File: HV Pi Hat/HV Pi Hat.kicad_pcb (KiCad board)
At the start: 4 copper layers, 85 x 56 mm, 20 parts, among them J1 B2B-XH-A_LF__SN_, J2 B2B-XH-A_LF__SN_, J3 SHV-R, J4 SHV-R

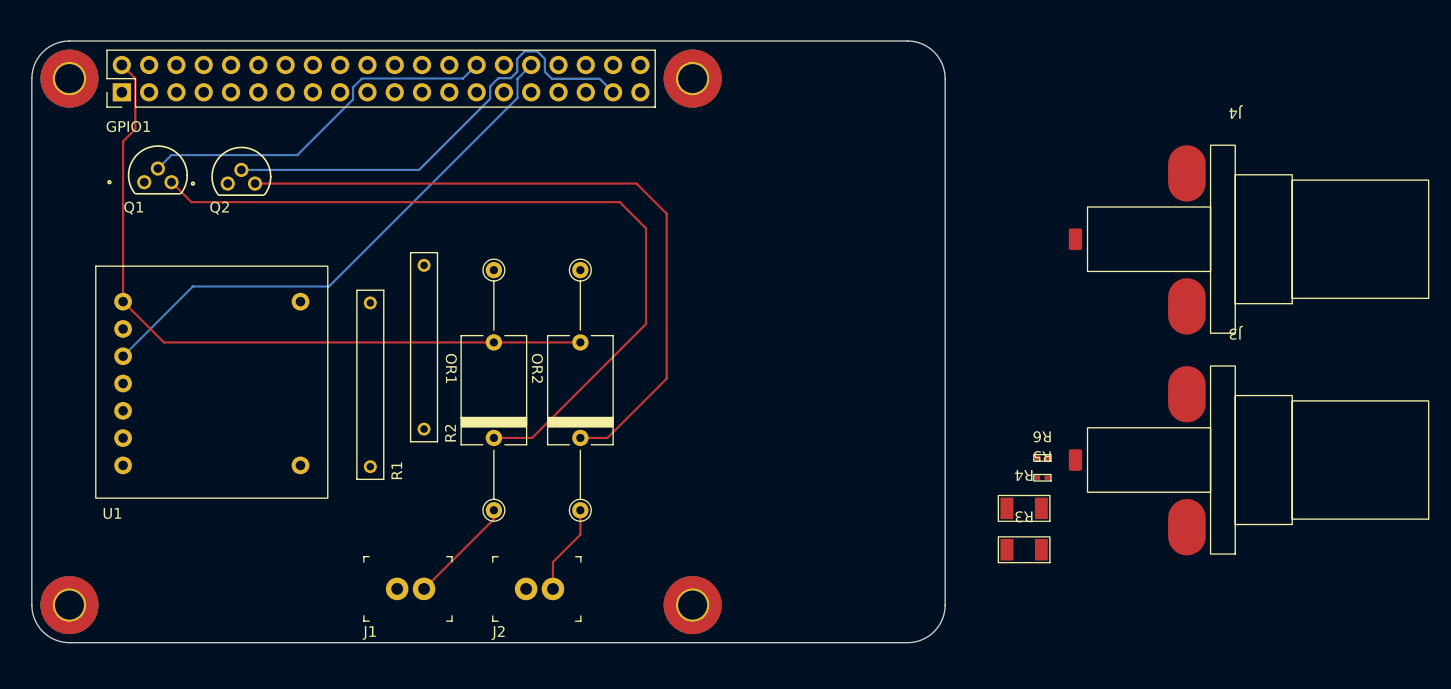
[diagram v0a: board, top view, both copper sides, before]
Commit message: Decision A1: HV Pi Hat autonomous build + HV/LV route pass
Schematic finalized to match CONTROL_DESIGN (netlist 30/30, ERC 0); PCB regenerated, placed, HV/LV lane-separated; HV routed on outer layers with inner-layer voids + GND guard pours; custom JLCPCB thick stackup + conformal-coat creepage (kicad_dru 2 mm air / 4 mm pour); sourced BOM; preliminary gerbers under fab/preliminary_DO_NOT_FAB; docs AUTONOMOUS_BUILD_LOG/BOM_SOURCED/HV_CONNECTOR_OPTIONS + updated STATUS/DECISIONS/EESCHEMA_TODO; toolchain now KiCad 10. Pending mandatory human-EE review before fab/energizing (5 kV).

Co-Authored-By: Claude Opus 4.8 (1M context) <noreply@anthropic.com>
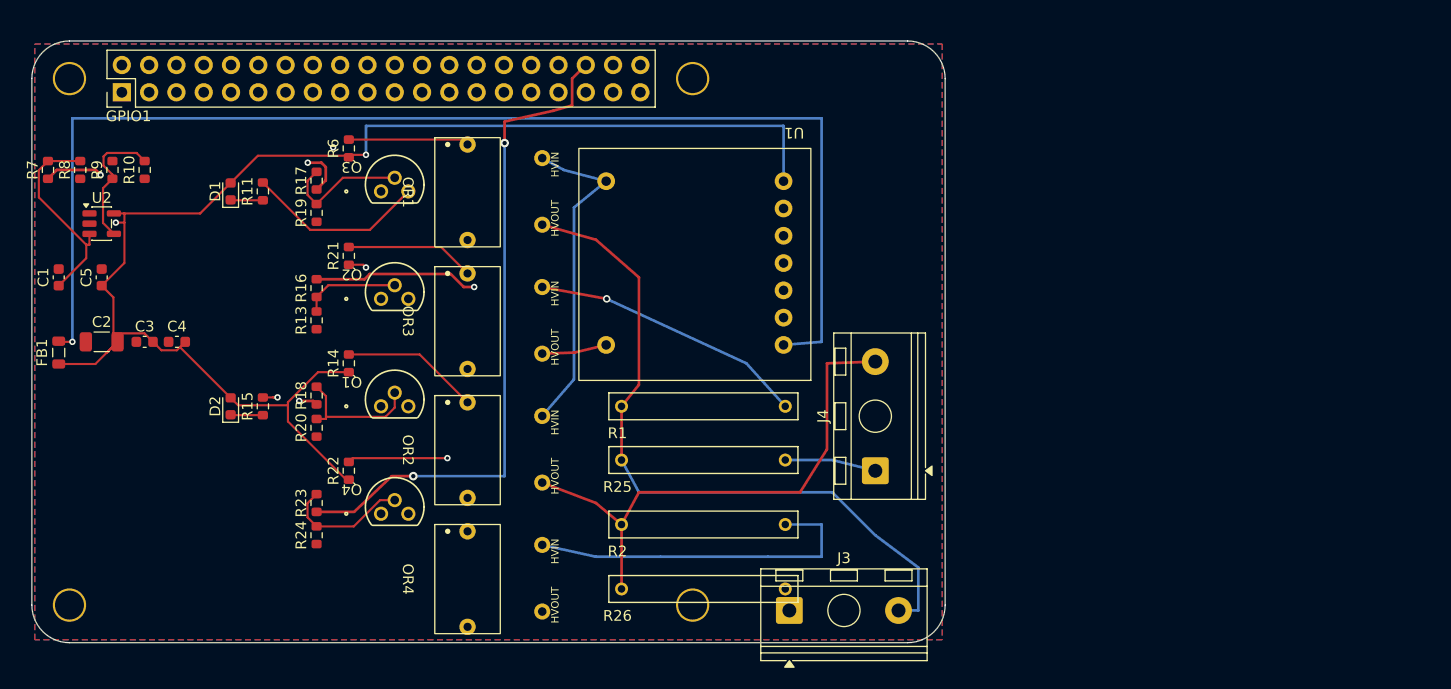
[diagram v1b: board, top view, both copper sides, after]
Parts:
- removed J1, J2: B2B-XH-A_LF__SN_, digikey-footprints:PinHeader_1x2_P2.5mm_Drill1.1mm
- removed R3, R4: 200, 3372-BND0603JKRS001TR-ND:Resistor 200 O
- removed R5: 300, 3372-CR0402FC300RS1TR-ND:Resistor 300 O
- added C1: 1 uF, Capacitor_SMD:C_0603_1608Metric, F.Cu at (120.0, 108.0)
- added C2: 47 uF, Capacitor_SMD:C_1206_3216Metric, F.Cu at (124.0, 114.0)
- added C3: 1 uF, Capacitor_SMD:C_0603_1608Metric, F.Cu at (128.0, 114.0)
- added C4: 0.1 uF, Capacitor_SMD:C_0603_1608Metric, F.Cu at (131.0, 114.0)
- added C5: 0.1 uF, Capacitor_SMD:C_0603_1608Metric, F.Cu at (124.0, 108.0)
- added D1: LED, LED_SMD:LED_0603_1608Metric, F.Cu at (136.0, 100.0)
- added D2: LED, LED_SMD:LED_0603_1608Metric, F.Cu at (136.0, 120.0)
- added FB1: FerriteBead, Inductor_SMD:L_0805_2012Metric, F.Cu at (120.0, 115.0)
- added OR3: ~, HV_Footprints:HVM OR-100, F.Cu at (155.0, 107.0)
- added OR4: ~, HV_Footprints:HVM OR-100, F.Cu at (155.0, 131.0)
- added Q3: ~, TN0610N3_G_P013_Footprint:TO-92_MC_MCH, F.Cu at (150.0, 100.0)
- added Q4: ~, TN0610N3_G_P013_Footprint:TO-92_MC_MCH, F.Cu at (150.0, 130.0)
- added R10: 10k, Resistor_SMD:R_0603_1608Metric, F.Cu at (128.0, 98.0)
- added R11: 470, Resistor_SMD:R_0603_1608Metric, F.Cu at (139.0, 100.0)
- added R13: 10k, Resistor_SMD:R_0603_1608Metric, F.Cu at (144.0, 112.0)
- added R14: 51, Resistor_SMD:R_0603_1608Metric, F.Cu at (147.0, 116.0)
- added R15: 470, Resistor_SMD:R_0603_1608Metric, F.Cu at (139.0, 120.0)
- added R16: 100, Resistor_SMD:R_0603_1608Metric, F.Cu at (144.0, 109.0)
- added R17: 100, Resistor_SMD:R_0603_1608Metric, F.Cu at (144.0, 99.0)
- added R18: 100, Resistor_SMD:R_0603_1608Metric, F.Cu at (144.0, 119.0)
- added R19: 10k, Resistor_SMD:R_0603_1608Metric, F.Cu at (144.0, 102.0)
- added R20: 10k, Resistor_SMD:R_0603_1608Metric, F.Cu at (144.0, 122.0)
- added R21: 51, Resistor_SMD:R_0603_1608Metric, F.Cu at (147.0, 106.0)
- added R22: 51, Resistor_SMD:R_0603_1608Metric, F.Cu at (147.0, 126.0)
- added R23: 100, Resistor_SMD:R_0603_1608Metric, F.Cu at (144.0, 129.0)
- added R24: 10k, Resistor_SMD:R_0603_1608Metric, F.Cu at (144.0, 132.0)
- added R25: 1G, MHR0317SA107F70:RESRR1524W50L1760T250H500, F.Cu at (180.0, 125.0)
- added R26: 1G, MHR0317SA107F70:RESRR1524W50L1760T250H500, F.Cu at (180.0, 137.0)
- added R7: 10k, Resistor_SMD:R_0603_1608Metric, F.Cu at (119.0, 98.0)
- added R8: 100k, Resistor_SMD:R_0603_1608Metric, F.Cu at (122.0, 98.0)
- added R9: 5.6k, Resistor_SMD:R_0603_1608Metric, F.Cu at (125.0, 98.0)
- added U2: MCP6001-OT, Package_TO_SOT_SMD:SOT-23-5, F.Cu at (124.0, 103.0)
- J3, J4: value SHV-R -> HV_Term_1x2; footprint 4912-SHV-R-ND:4912-SHV-R-ND -> TerminalBlock_RND:TerminalBlock_RND_205-00241_1x02_P10.16mm_Horizontal
- R6: value 300 -> 51; footprint 3372-CR0402FC300RS1TR-ND:Resistor 300 O -> Resistor_SMD:R_0603_1608Metric
- moved U1 74.1 mm to (190.0, 96.0), turned to 180 degrees
- moved R6 70.7 mm to (147.0, 96.0), turned to 90 degrees
- moved J3 43.8 mm to (188.0, 139.0), turned to 0 degrees
- moved J4 39.8 mm to (196.0, 126.0), turned to 90 degrees
- moved R1 31.1 mm to (180.0, 120.0), turned to 0 degrees
- moved R2 30.8 mm to (180.0, 131.0), turned to 0 degrees
- moved Q1 30.3 mm to (150.0, 120.0)
- moved OR1 18.6 mm to (155.0, 95.0)
- moved Q2 17.9 mm to (150.0, 110.0)
- moved OR2 11.9 mm to (155.0, 119.0)
- renumbered REF** to H1, REF** to H2, REF** to H3, REF** to H4
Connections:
- net Net-(OR1-HVIN) renamed /HV_RAIL
- GPIO1 pad 28: Net-(GPIO1-GPIO_1) -> unconnected-(GPIO1-GPIO_1-Pad28)
- GPIO1 pad 29: unconnected-(GPIO1-GPIO_5-Pad29) -> /GPIO_5
- GPIO1 pad 31: unconnected-(GPIO1-GPIO_6-Pad31) -> /GPIO_6
- GPIO1 pad 32: Net-(GPIO1-GPIO_12) -> /GPIO_12
- GPIO1 pad 36: unconnected-(GPIO1-GPIO_16-Pad36) -> /GPIO_16
- GPIO1 pad 37: Net-(GPIO1-GPIO_26) -> /GPIO_26
- J3 pad 1: Net-(J3-Pin_1) -> GND
- J3 pad 2: /<NO NET> -> /HV_CH1
- J4 pad 1: Net-(J4-Pin_1) -> GND
- J4 pad 2: Net-(J4-Pin_2) -> /HV_CH2
- OR1 pad 1: Net-(OR1-GND) -> /CH1_CHG_DRN
- OR1 pad 4: /<NO NET> -> /HV_CH1
- OR2 pad 1: Net-(OR2-GND) -> /CH2_CHG_DRN
- OR2 pad 2: Net-(OR2-LED+) -> /CH2_CHG_LED
- OR2 pad 4: Net-(J4-Pin_2) -> /HV_CH2
- Q1 pad 2: Net-(GPIO1-GPIO_1) -> /CH2_CHG_GATE
- Q1 pad 3: Net-(OR1-GND) -> /CH2_CHG_DRN
- Q2 pad 2: Net-(GPIO1-GPIO_26) -> /CH1_DIS_GATE
- Q2 pad 3: Net-(OR2-GND) -> /CH1_DIS_DRN
- R1 pad 1: Net-(J3-Pin_1) -> /HV_CH1
- R1 pad 2: GND -> /HV_CH1_DIS
- R2 pad 1: Net-(J4-Pin_1) -> /HV_CH2
- R2 pad 2: GND -> /HV_CH2_DIS
- R6 pad 2: Net-(D1-A) -> Net-(OR1-LED+)
- U1 pad 1: +5V -> Net-(U1-VIN)
- U1 pad 3: Net-(GPIO1-GPIO_12) -> /GPIO_12_Boost
- U1 pad 7: unconnected-(U1-ILIMIT-Pad7) -> +5V
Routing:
- net Net-(U1-VIN): track 0.00 -> 118.0 mm, vias 0 -> 1
- net +5V: track 67.1 -> 166.2 mm, vias 0 -> 3
- net Net-(OR1-GND): track 73.4 -> 0.00 mm
- net /HV_CH1: track 0.00 -> 66.0 mm
- net Net-(OR2-GND): track 65.1 -> 0.00 mm
- net /GPIO_16: track 0.00 -> 62.6 mm, vias 0 -> 2
- net /GPIO_26: track 0.00 -> 57.8 mm, vias 0 -> 2
- net /GPIO_12: track 0.00 -> 53.1 mm, vias 0 -> 1
- net GND: track 67.5 -> 14.5 mm
- net Net-(GPIO1-GPIO_12): track 50.3 -> 0.00 mm
- net /HV_CH2: track 0.00 -> 50.1 mm
- net Net-(GPIO1-GPIO_26): track 42.8 -> 0.00 mm
- net /GPIO_6: track 0.00 -> 35.7 mm, vias 0 -> 1
- net Net-(GPIO1-GPIO_1): track 34.3 -> 0.00 mm
- net /HV_CH2_DIS: track 0.00 -> 32.5 mm
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- added copper zone on B.Cu, net GND
- added copper zone on F.Cu, net GND
- removed copper zone on In2.Cu, net GND
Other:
- board text added: "Pi5 USB-A/RJ45 below -> use >=20mm standoffs + tall GPIO header"

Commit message: Route PGM, reconnect op-amp ground, set JLC 7628D stackup
- Route /GPIO_12_Boost (op-amp out U2.1, feedback R9.2, SMHV0550 PGM
  U1.3). It was unrouted, so the board had no HV setpoint path. The
  route stays on the LV side and enters the module along its LV pin
  column, 2 mm or more from all HV copper.
- Add a GND stitching via for the F.Cu pour island holding U2.2 (op-amp
  GND) and R8.1 (100 k PGM pulldown). The island was cut off from GND,
  so the op-amp had no return and the PGM-low-at-boot fail-safe did not
  work.
- Remove dangling and duplicate LV stub segments; solid zone connection
  on the Q1/Q3 GND pads (starved thermals).
- Stackup: JLCPCB JLC04201H-7628D (0.864 mm outer prepreg, 0.2 mm core,
  2.0 mm nominal), replacing the default 1.6 mm stack (ADR-0002).
- Regenerate fab/BOM.csv from the schematic (J3/J4 were still SHV-R)
  and the top/bottom renders.
- Add tools/HvInterlayer.py: smallest 3-D HV-to-LV distances across
  layers, which the 2-D DRC cannot check.

DRC (kicad-cli 10.0.1): 0 unconnected, 0 HV clearance or creepage at
the provisional 2 mm rules. Remaining: R26 courtyard vs H4/J3, mounting
hole library mismatch (intentional), silkscreen.

Co-Authored-By: Claude Opus 5.5 <noreply@anthropic.com>
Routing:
- net /GPIO_12_Boost: track 0.00 -> 103.6 mm, vias 0 -> 3
- net +5V: track 166.2 -> 157.4 mm
- net /GPIO_12: track 53.1 -> 50.4 mm
- net /GPIO_26: track 57.8 -> 55.4 mm
- net Net-(U1-VIN): track 118.0 -> 116.2 mm
- net /CH2_CHG_DRN: track 27.1 -> 26.3 mm
- net GND: vias 0 -> 1
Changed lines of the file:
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@@
 	(generator_version "10.0")
 	(general
-		(thickness 1.6)
+		(thickness 2.0484)
 		(legacy_teardrops no)
 	)
@@
 			(layer "dielectric 1"
 				(type "prepreg")
-				(thickness 0.1)
-				(material "FR4")
-				(epsilon_r 4.5)
+				(thickness 0.864)
+				(material "FR4 7628x4")
+				(epsilon_r 4.4)
 				(loss_tangent 0.02)
 			)
 			(layer "In1.Cu"
 				(type "copper")
-				(thickness 0.035)
+				(thickness 0.0152)
 			)
 			(layer "dielectric 2"
 				(type "core")
-				(thickness 1.24)
+				(thickness 0.2)
 				(material "FR4")
-				(epsilon_r 4.5)
+				(epsilon_r 4.6)
 				(loss_tangent 0.02)
 			)
 			(layer "In2.Cu"
 				(type "copper")
-				(thickness 0.035)
+				(thickness 0.0152)
 			)
 			(layer "dielectric 3"
 				(type "prepreg")
-				(thickness 0.1)
-				(material "FR4")
-				(epsilon_r 4.5)
+				(thickness 0.864)
+				(material "FR4 7628x4")
+				(epsilon_r 4.4)
 				(loss_tangent 0.02)
 			)
@@
 			(remove_unused_layers no)
 			(net "GND")
+			(zone_connect 2)
 		)
 		(pad "2" thru_hole circle
@@
 			(remove_unused_layers no)
 			(net "GND")
+			(zone_connect 2)
 		)
 		(pad "2" thru_hole circle
@@
 		(net "GND")
 	)
+	(via
+		(at 122.100299 100.977499)
+		(size 0.6)
+		(drill 0.3)
+		(layers "F.Cu" "B.Cu")
+		(net "GND")
+	)
 	(segment
 		(start 192 125)
@@
 		(net "/CH2_CHG_DRN")
 	)
-	(segment
-		(start 140.3658 119.1684)
-		(end 139.9835 119.1684)
-		(width 0.2)
-		(layer "F.Cu")
-		(net "/CH2_CHG_DRN")
-	)
 	(via
 		(at 140.3658 119.1684)
@@
 	)
 	(segment
-		(start 139.9835 119.1684)
-		(end 140.3658 119.1684)
-		(width 0.2)
-		(layer "In2.Cu")
-		(net "/CH2_CHG_DRN")
-	)
-	(segment
 		(start 142.2076 121.0102)
 		(end 140.3658 119.1684)
@@
 	)
 	(segment
-		(start 124.4438 115.0312)
-		(end 125.0915 114.3835)
-		(width 0.2)
-		(layer "F.Cu")
-		(net "+5V")
-	)
-	(segment
 		(start 148.5969 96.5948)
 		(end 147.2302 96.5948)
@@
 	)
 	(segment
-		(start 129.0629 114.2879)
-		(end 129.063 114.2879)
-		(width 0.2)
-		(layer "F.Cu")
-		(net "+5V")
-	)
-	(segment
 		(start 147 126.825)
 		(end 146.7525 126.825)
@@
 	)
 	(segment
-		(start 154.7162 100.8155)
-		(end 150.4955 96.5948)
-		(width 0.2)
-		(layer "In2.Cu")
-		(net "+5V")
-	)
-	(segment
-		(start 150.4955 96.5948)
-		(end 148.5969 96.5948)
-		(width 0.2)
-		(layer "In2.Cu")
-		(net "+5V")
-	)
-	(segment
 		(start 121.2749 113.9999)
 		(end 120.0624 113.9999)
@@
 		(net "Net-(U1-VIN)")
 	)
-	(segment
-		(start 120.0624 113.9999)
-		(end 120 113.9375)
-		(width 0.2)
-		(layer "F.Cu")
-		(net "Net-(U1-VIN)")
-	)
-	(segment
-		(start 121.2749 113.9999)
-		(end 121.1233 113.9999)
-		(width 0.2)
-		(layer "F.Cu")
-		(net "Net-(U1-VIN)")
-	)
-	(segment
-		(start 121.1233 113.9999)
-		(end 121.2749 113.9999)
-		(width 0.2)
-		(layer "F.Cu")
-		(net "Net-(U1-VIN)")
-	)
 	(via
 		(at 121.2749 113.9999)
@@
 	)
 	(segment
-		(start 122.1496 113.1252)
-		(end 121.2749 113.9999)
-		(width 0.2)
-		(layer "In2.Cu")
-		(net "Net-(U1-VIN)")
-	)
-	(segment
 		(start 121.2749 113.9999)
 		(end 121.1233 113.9999)
@@
 	)
 	(segment
-		(start 121.1233 113.9999)
-		(end 121.2749 113.9999)
-		(width 0.2)
-		(layer "In2.Cu")
-		(net "Net-(U1-VIN)")
+		(start 124.975 97.175)
+		(end 126.875 97.175)
+		(width 0.254)
+		(layer "F.Cu")
+		(net "/GPIO_12_Boost")
+	)
+	(segment
+		(start 164.475 93.875)
+		(end 185.875 94.375)
+		(width 0.254)
+		(layer "F.Cu")
+		(net "/GPIO_12_Boost")
+	)
+	(segment
+		(start 186.175 107.675)
+		(end 187.475 109.175)
+		(width 0.254)
+		(layer "F.Cu")
+		(net "/GPIO_12_Boost")
+	)
+	(segment
+		(start 185.875 94.375)
+		(end 185.975 94.475)
+		(width 0.254)
+		(layer "F.Cu")
+		(net "/GPIO_12_Boost")
+	)
+	(segment
+		(start 185.975 94.475)
+		(end 186.175 107.675)
+		(width 0.254)
+		(layer "F.Cu")
+		(net "/GPIO_12_Boost")
+	)
+	(segment
+		(start 163.575 93.975)
+		(end 164.475 93.875)
+		(width 0.254)
+		(layer "F.Cu")
+		(net "/GPIO_12_Boost")
+	)
+	(segment
+		(start 122.875 102.074999)
+		(end 123.375 102.074999)
+		(width 0.254)
+		(layer "F.Cu")
+		(net "/GPIO_12_Boost")
+	)
+	(segment
+		(start 163.175 94.175)
+		(end 163.575 93.975)
+		(width 0.254)
+		(layer "F.Cu")
+		(net "/GPIO_12_Boost")
+	)
+	(segment
+		(start 162.375 94.675)
+		(end 163.175 94.175)
+		(width 0.254)
+		(layer "F.Cu")
+		(net "/GPIO_12_Boost")
+	)
+	(via
+		(at 126.875 97.175)
+		(size 0.6)
+		(drill 0.3)
+		(layers "F.Cu" "B.Cu")
+		(net "/GPIO_12_Boost")
+	)
+	(via
+		(at 162.375 94.675)
+		(size 0.6)
+		(drill 0.3)
+		(layers "F.Cu" "B.Cu")
+		(net "/GPIO_12_Boost")
+	)
+	(via
+		(at 123.375 102.074999)
+		(size 0.6)
+		(drill 0.3)
+		(layers "F.Cu" "B.Cu")
+		(net "/GPIO_12_Boost")
+	)
+	(segment
+		(start 126.875 97.175)
+		(end 144.275 96.574999)
+		(width 0.254)
+		(layer "B.Cu")
+		(net "/GPIO_12_Boost")
+	)
+	(segment
+		(start 123.375 102.074999)
+		(end 148.575 97.375)
+		(width 0.254)
+		(layer "B.Cu")
+		(net "/GPIO_12_Boost")
+	)
+	(segment
+		(start 161.375 94.574999)
+		(end 162.375 94.675)
+		(width 0.254)
+		(layer "B.Cu")
+		(net "/GPIO_12_Boost")
+	)
+	(segment
+		(start 158.975 96.875)
+		(end 160.975 94.774999)
+		(width 0.254)
+		(layer "B.Cu")
+		(net "/GPIO_12_Boost")
+	)
+	(segment
+		(start 144.275 96.574999)
+		(end 148.575 97.375)
+		(width 0.254)
+		(layer "B.Cu")
+		(net "/GPIO_12_Boost")
+	)
+	(segment
+		(start 148.575 97.375)
+		(end 158.975 96.875)
+		(width 0.254)
+		(layer "B.Cu")
+		(net "/GPIO_12_Boost")
+	)
+	(segment
+		(start 160.975 94.774999)
+		(end 161.375 94.574999)
+		(width 0.254)
+		(layer "B.Cu")
+		(net "/GPIO_12_Boost")
 	)
 	(segment
@@
 		(net "/GPIO_5")
 	)
-	(segment
-		(start 143.295 97.3282)
-		(end 143.1756 97.3282)
-		(width 0.254)
-		(layer "F.Cu")
-		(net "/GPIO_5")
-	)
 	(via
 		(at 143.1756 97.3282)
@@
 	)
 	(segment
-		(start 143.1756 97.3282)
-		(end 143.295 97.3282)
-		(width 0.254)
-		(layer "In2.Cu")
-		(net "/GPIO_5")
-	)
-	(segment
 		(start 143.1756 97.3059)
 		(end 143.1756 97.3282)
@@
 		(net "/GPIO_12")
 	)
-	(segment
-		(start 123.9001 98.4786)
-		(end 123.4215 98)
-		(width 0.254)
-		(layer "F.Cu")
-		(net "/GPIO_12")
-	)
-	(segment
-		(start 123.4215 98)
-		(end 123.9001 98.4786)
-		(width 0.254)
-		(layer "F.Cu")
-		(net "/GPIO_12")
-	)
 	(via
 		(at 123.9001 98.4786)
@@
 	)
 	(segment
-		(start 123.4215 98)
-		(end 123.9001 98.4786)
-		(width 0.254)
-		(layer "In2.Cu")
-		(net "/GPIO_12")
-	)
-	(segment
 		(start 160.165 90.2291)
 		(end 160.165 91.3373)
@@
 	)
 	(segment
-		(start 123.9001 98.4786)
-		(end 123.4215 98)
-		(width 0.254)
-		(layer "In2.Cu")
-		(net "/GPIO_12")
-	)
-	(segment
 		(start 130.1604 92.2183)
 		(end 123.9001 98.4786)
@@
 	)
 	(segment
-		(start 145.9627 95.4786)
-		(end 145.5409 95.9004)
-		(width 0.254)
-		(layer "In1.Cu")
-		(net "/GPIO_26")
-	)
-	(segment
 		(start 143.5914 95.9004)
 		(end 142.3822 97.1096)
@@
 	)
 	(segment
-		(start 145.5409 95.9004)
-		(end 145.9627 95.4786)
-		(width 0.254)
-		(layer "In1.Cu")
-		(net "/GPIO_26")
-	)
-	(segment
-		(start 145.5409 95.9004)
-		(end 145.9627 95.4786)
-		(width 0.254)
-		(layer "In2.Cu")
-		(net "/GPIO_26")
-	)
-	(segment
 		(start 168 92.8)
 		(end 171.59 90.78)
@@
 		(layer "In2.Cu")
 		(net "/GPIO_26")
-	)
-	(segment
-		(start 145.9627 95.4786)
-		(end 145.5409 95.9004)
-		(width 0.254)
-		(layer "In2.Cu")
-		(net "/GPIO_26")
